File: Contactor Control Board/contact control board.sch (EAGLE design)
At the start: 29 parts, among them K1 DS2Y-S-DC5V, Q1 2n2222, Q3 2n2222, Q4 MOSFET-NCHANNELFQP30N06L, U1 LM393AN

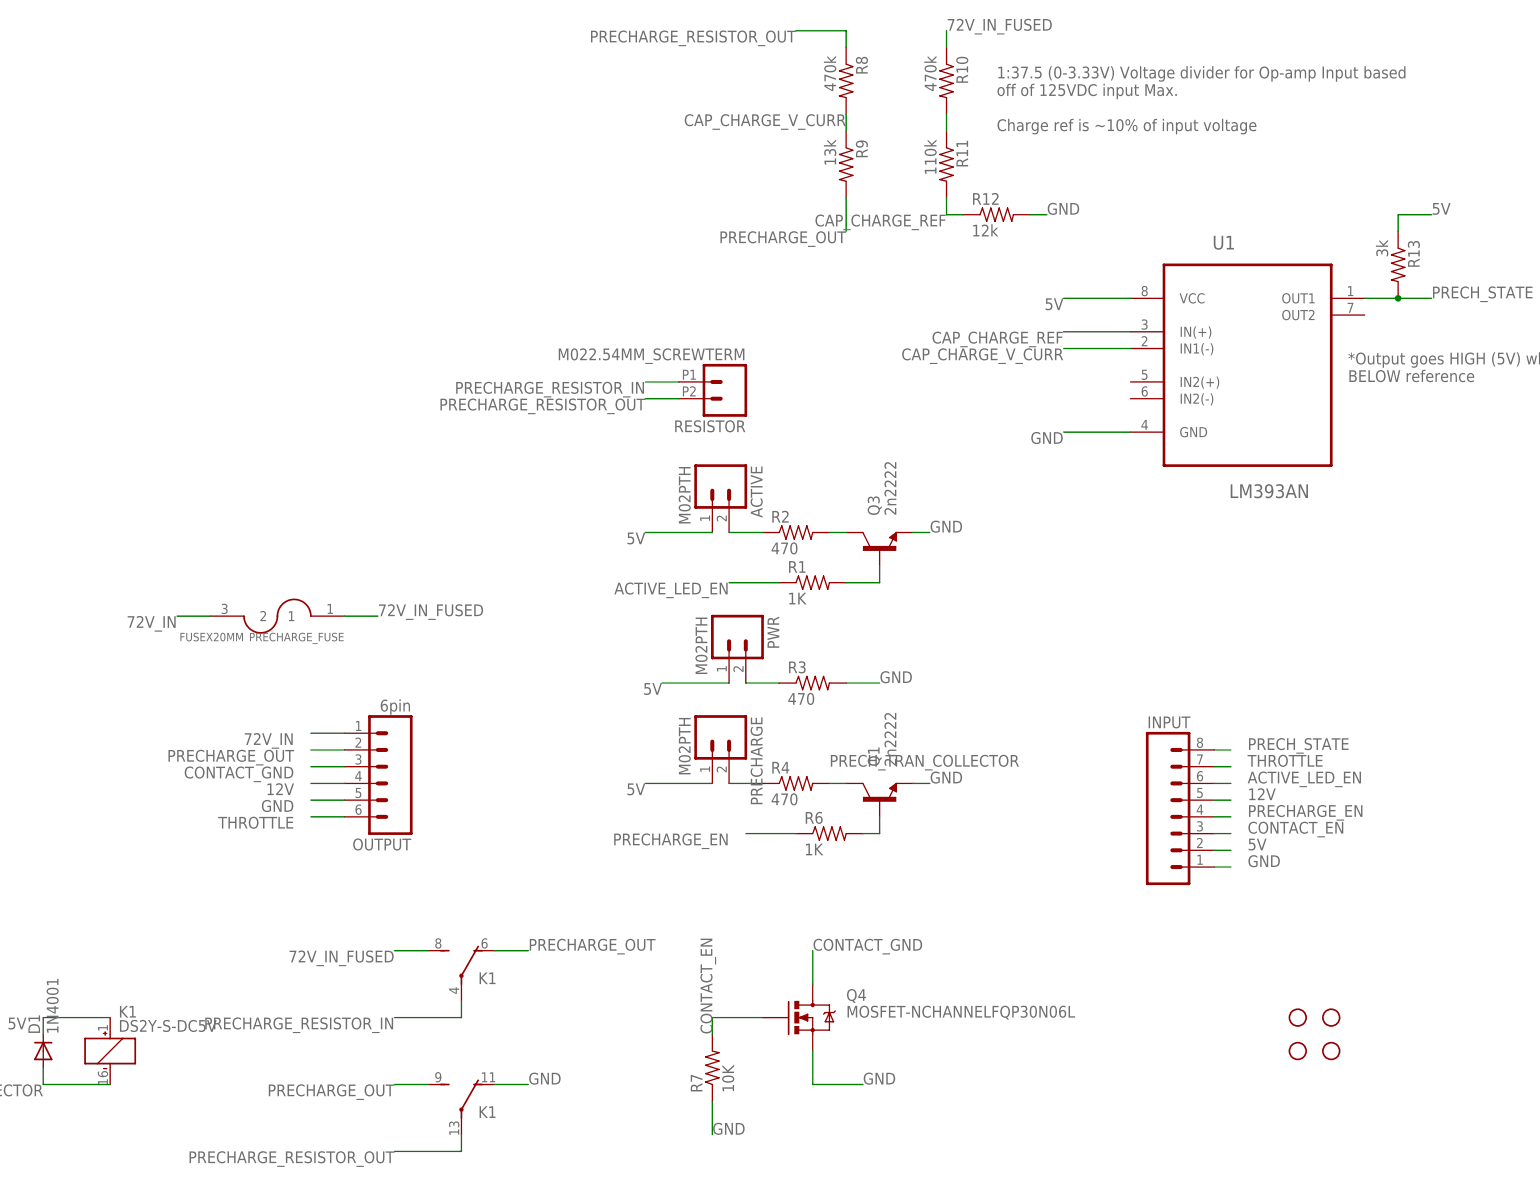
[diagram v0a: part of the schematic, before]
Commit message: Deleting SMD variant of the CCB for now.
Keeping the two boards in design sync while iterating on one wasn't a
smart idea. Conversion will happen once the CCB has been validated using
proto-boards. Did a test route of the CCB using thru-hole parts in a
2"x3" space and there's a ton of room. Cool!
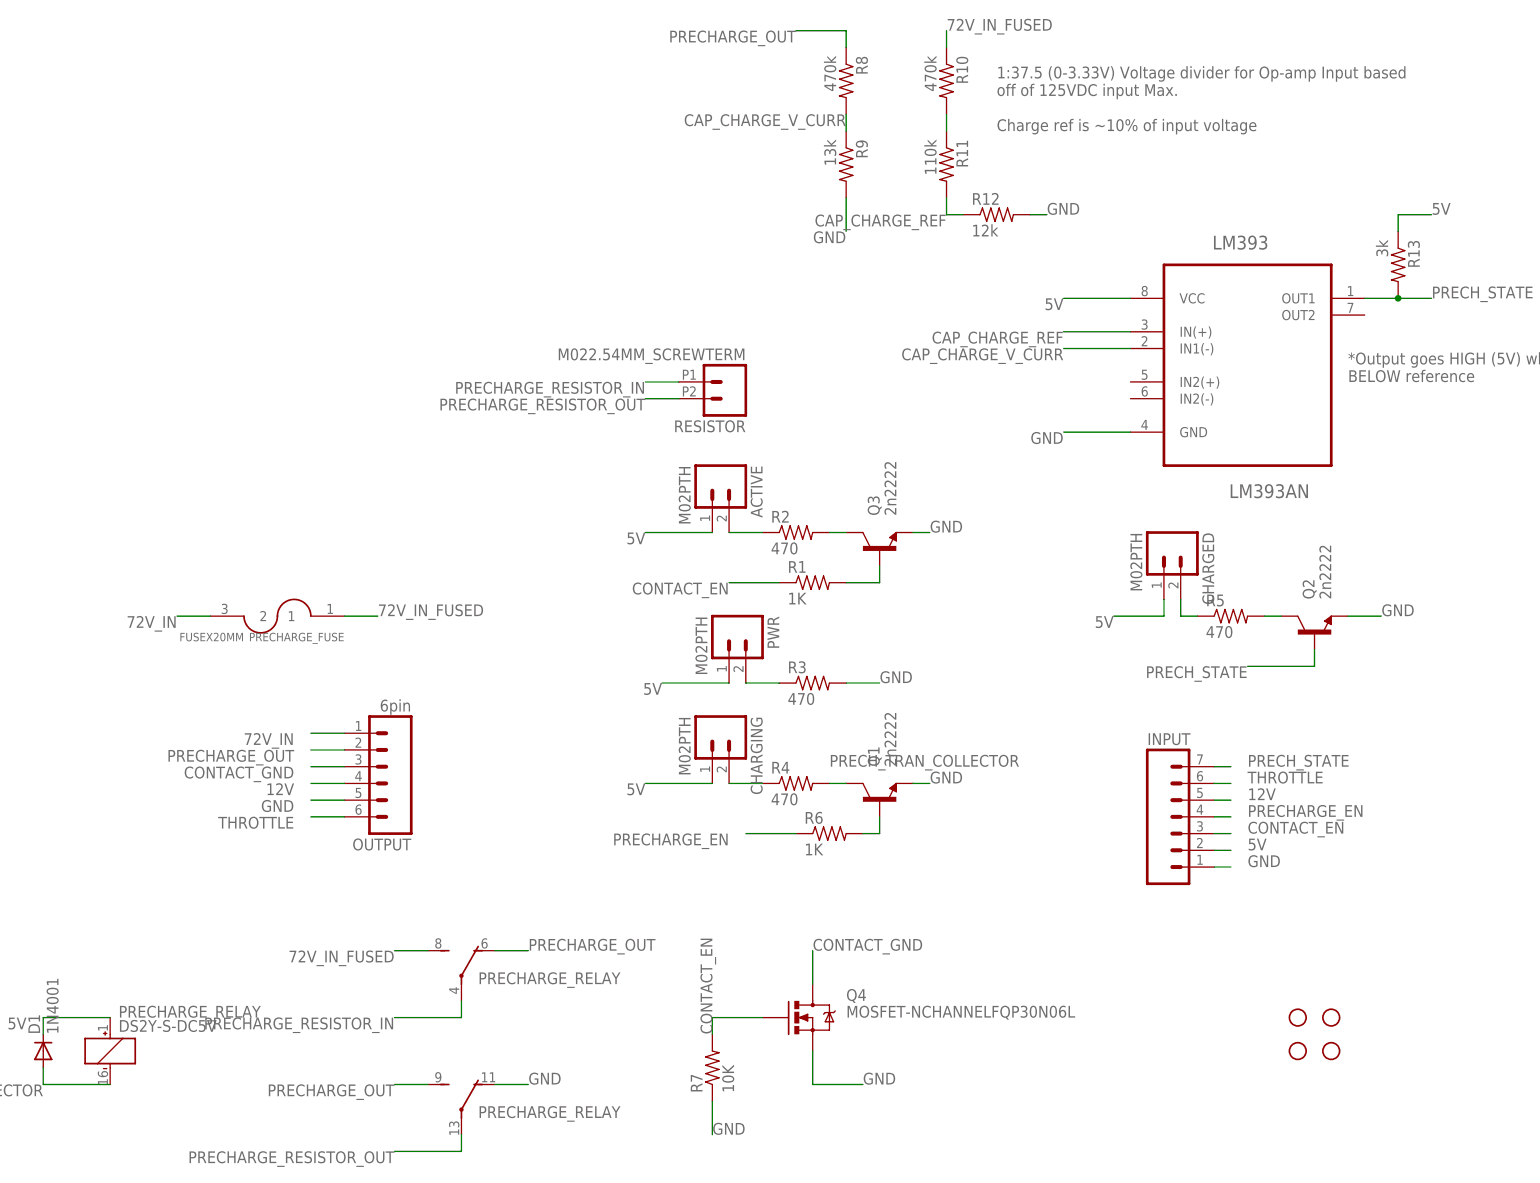
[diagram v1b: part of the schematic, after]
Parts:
- added CHARGED: M02PTH, SparkFun-Connectors:M02PTH
- added Q2: 2n2222, SparkFun-DiscreteSemi:TRANSISTOR_NPNTO92
- added R5: 470, SparkFun-Resistors:RESISTORPTH-1/4W
- INPUT: device SparkFun-Connectors:M081X08 -> SparkFun-Connectors:M07
- renumbered K1 to PRECHARGE_RELAY, PRECHARGE to CHARGING, U1 to LM393
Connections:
- removed net ACTIVE_LED_EN: INPUT.6, R1.1
- new net N$4: CHARGED.2, R5.1
- new net N$5: Q2.C, R5.2
- net 5V: now also CHARGED.1
- net CONTACT_EN: now also R1.1
- net GND: now also Q2.E, R9.2
- net PRECHARGE_OUT: now also R8.1; no longer R9.2
- net PRECHARGE_RESISTOR_OUT: no longer R8.1
- net PRECH_STATE: now also INPUT.7, Q2.B; no longer INPUT.8
- net THROTTLE: now also INPUT.6; no longer INPUT.7

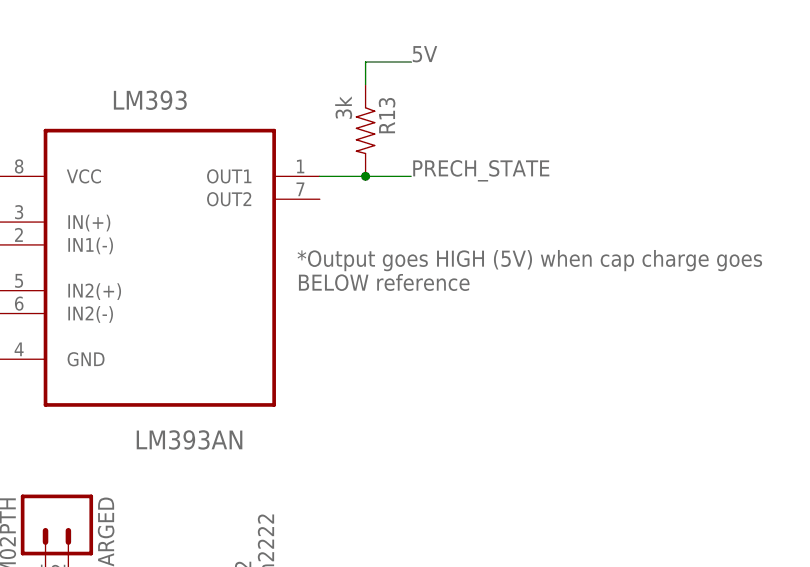
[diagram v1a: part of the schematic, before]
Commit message: Fixing bad note in design
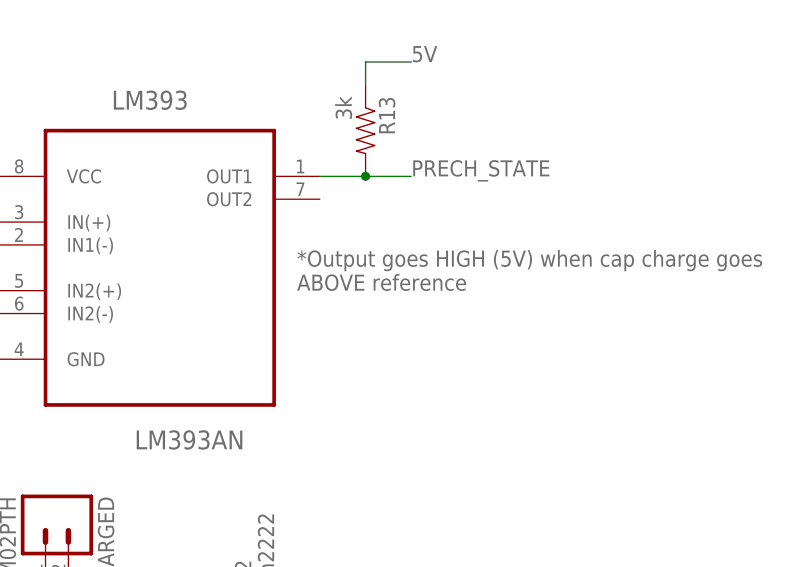
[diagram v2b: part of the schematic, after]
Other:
- note added: "*Output goes HIGH (5V) when cap charge goes ABOVE reference"
- note removed: "*Output goes HIGH (5V) when cap charge goes BELOW reference"
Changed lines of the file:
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@@
 Charge ref is ~10% of input voltage</text>
 <text x="147.32" y="114.3" size="1.778" layer="95">*Output goes HIGH (5V) when cap charge goes
-BELOW reference</text>
+ABOVE reference</text>
 </plain>
 <instances>

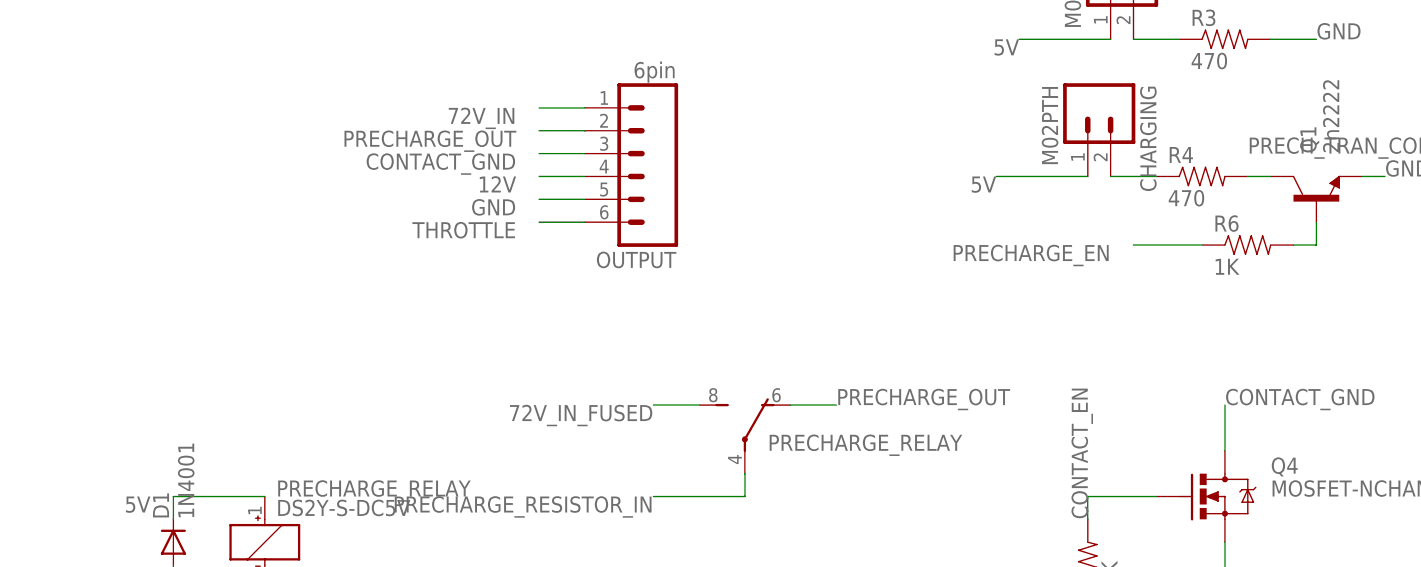
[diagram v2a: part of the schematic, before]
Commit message: Added BMS interface board and updated CCB with current limiting resistor
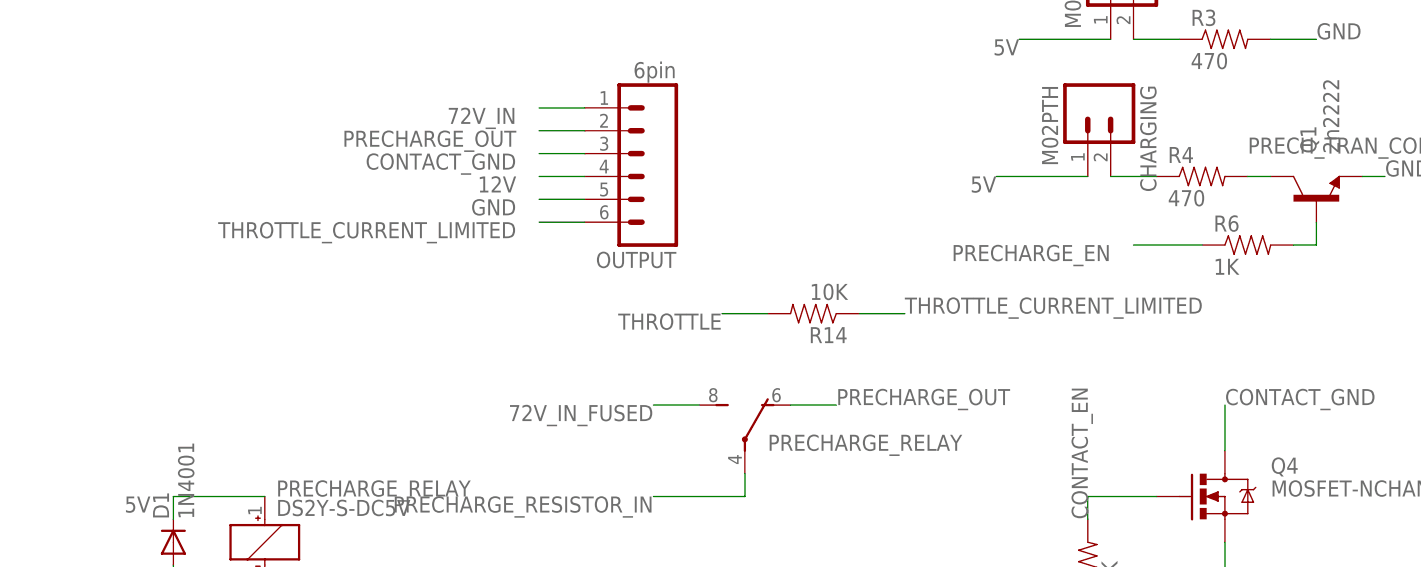
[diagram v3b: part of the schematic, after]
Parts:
- added R14: 10K, SparkFun-Resistors:RESISTORPTH-1/4W
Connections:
- new net THROTTLE_CURRENT_LIMITED: OUTPUT.6, R14.1
- net THROTTLE: now also R14.2; no longer OUTPUT.6
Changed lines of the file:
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@@
 <part name="Q2" library="SparkFun-DiscreteSemi" deviceset="TRANSISTOR_NPN" device="TO92" value="2n2222"/>
 <part name="R5" library="SparkFun-Resistors" deviceset="RESISTOR" device="PTH-1/4W" value="470"/>
+<part name="R14" library="SparkFun-Resistors" deviceset="RESISTOR" device="PTH-1/4W" value="10K"/>
 </parts>
 <sheets>
@@
 <instance part="Q2" gate="G$1" x="142.24" y="76.2" rot="R90"/>
 <instance part="R5" gate="G$1" x="129.54" y="78.74"/>
+<instance part="R14" gate="G$1" x="20.32" y="38.1" rot="R180"/>
 </instances>
 <busses>
@@
 <net name="THROTTLE" class="0">
 <segment>
-<pinref part="OUTPUT" gate="G$1" pin="6"/>
-<wire x1="-5.08" y1="48.26" x2="-10.16" y2="48.26" width="0.2032" layer="91"/>
-<label x="-12.7" y="48.26" size="1.778" layer="95" rot="R180"/>
-</segment>
-<segment>
 <wire x1="127" y1="53.34" x2="129.54" y2="53.34" width="0.2032" layer="91"/>
 <label x="132.08" y="53.34" size="1.778" layer="95"/>
 <pinref part="INPUT" gate="G$1" pin="6"/>
+</segment>
+<segment>
+<pinref part="R14" gate="G$1" pin="2"/>
+<wire x1="15.24" y1="38.1" x2="10.16" y2="38.1" width="0.2032" layer="91"/>
+<label x="10.16" y="38.1" size="1.778" layer="95" rot="R180"/>
 </segment>
 </net>
@@
 </segment>
 </net>
+<net name="THROTTLE_CURRENT_LIMITED" class="0">
+<segment>
+<pinref part="OUTPUT" gate="G$1" pin="6"/>
+<wire x1="-5.08" y1="48.26" x2="-10.16" y2="48.26" width="0.2032" layer="91"/>
+<label x="-12.7" y="48.26" size="1.778" layer="95" rot="R180"/>
+</segment>
+<segment>
+<pinref part="R14" gate="G$1" pin="1"/>
+<wire x1="25.4" y1="38.1" x2="30.48" y2="38.1" width="0.2032" layer="91"/>
+<label x="30.48" y="38.1" size="1.778" layer="95"/>
+</segment>
+</net>

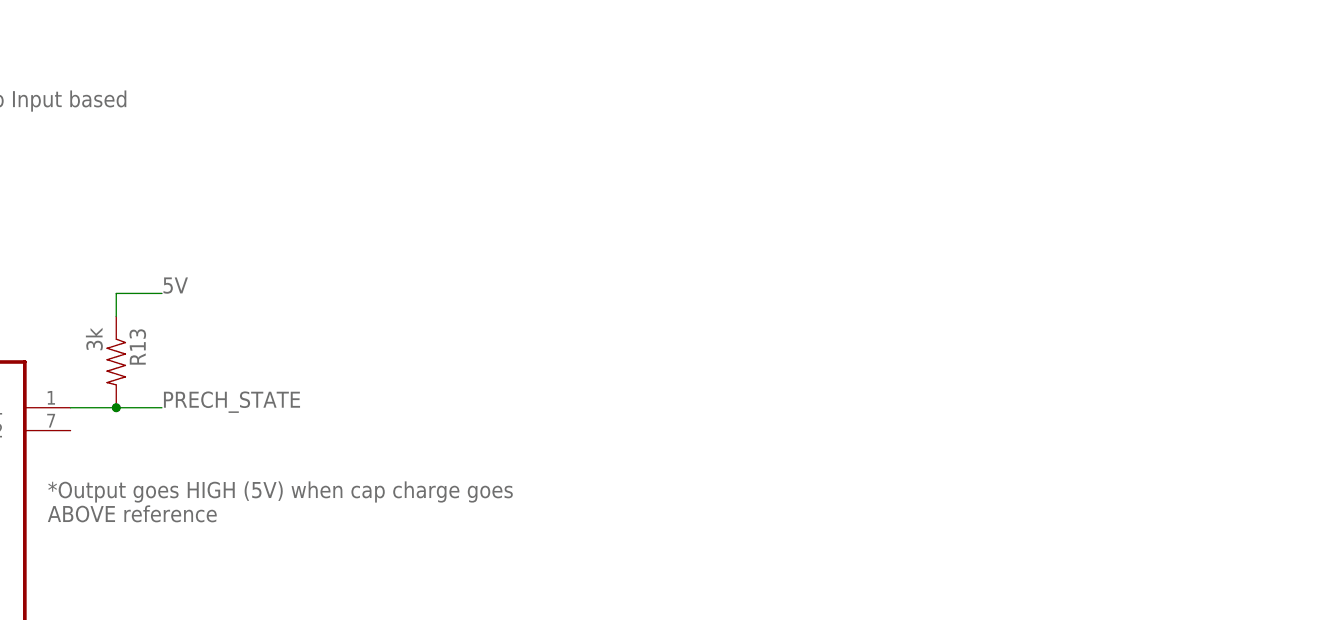
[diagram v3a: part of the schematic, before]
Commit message: Opto-coupling precharge signal with op-amp output
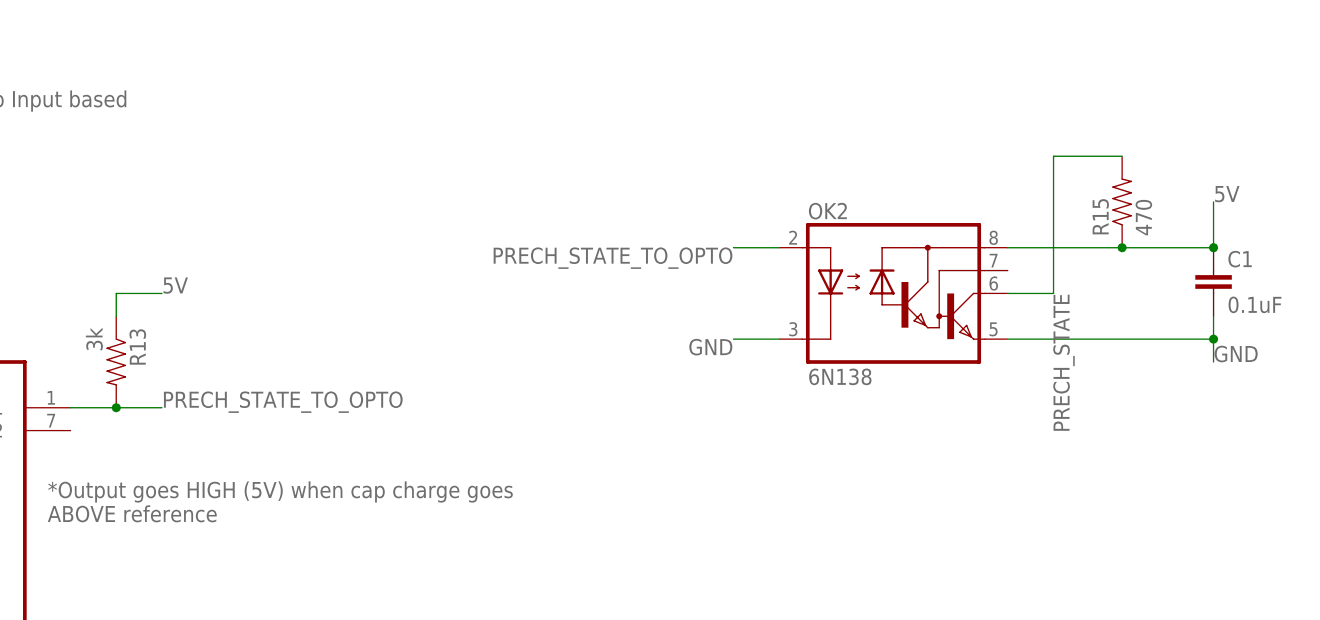
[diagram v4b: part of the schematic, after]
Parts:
- added C1: 0.1uF, SparkFun-Capacitors:CAP0603-CAP
- added OK2: 6N138, optocoupler:6N138
- added R15: 470, SparkFun-Resistors:RESISTORPTH-1/4W
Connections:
- new net PRECH_STATE_TO_OPTO: LM393.OUT1, OK2.A, R13.2
- net 5V: now also C1.1, OK2.VCC, R15.1
- net GND: now also C1.2, OK2.C, OK2.GND
- net PRECH_STATE: now also OK2.VO, R15.2; no longer LM393.OUT1, R13.2
